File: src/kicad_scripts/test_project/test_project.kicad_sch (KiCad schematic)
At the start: 256 parts

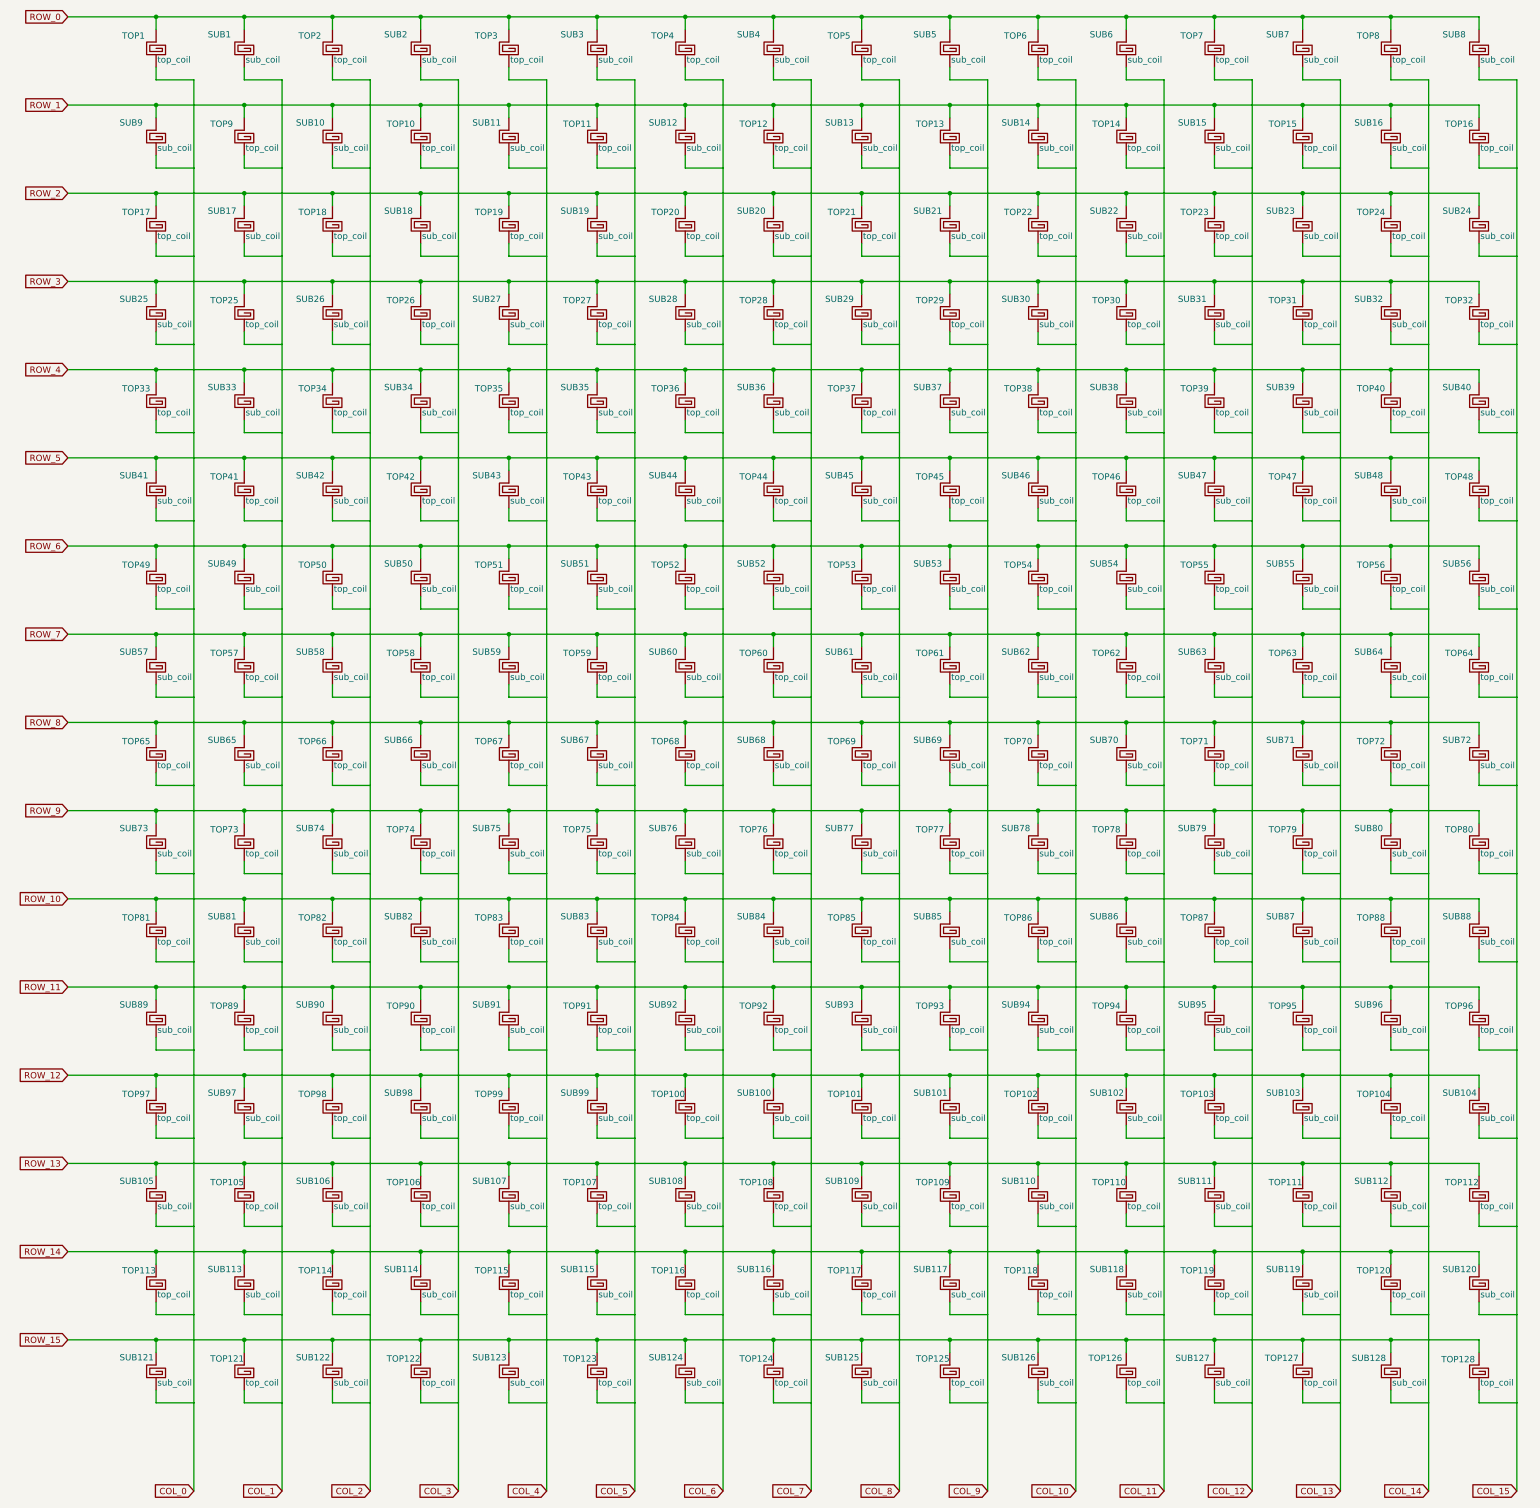
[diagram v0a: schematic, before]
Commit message: Added test project, lets go by hand for now
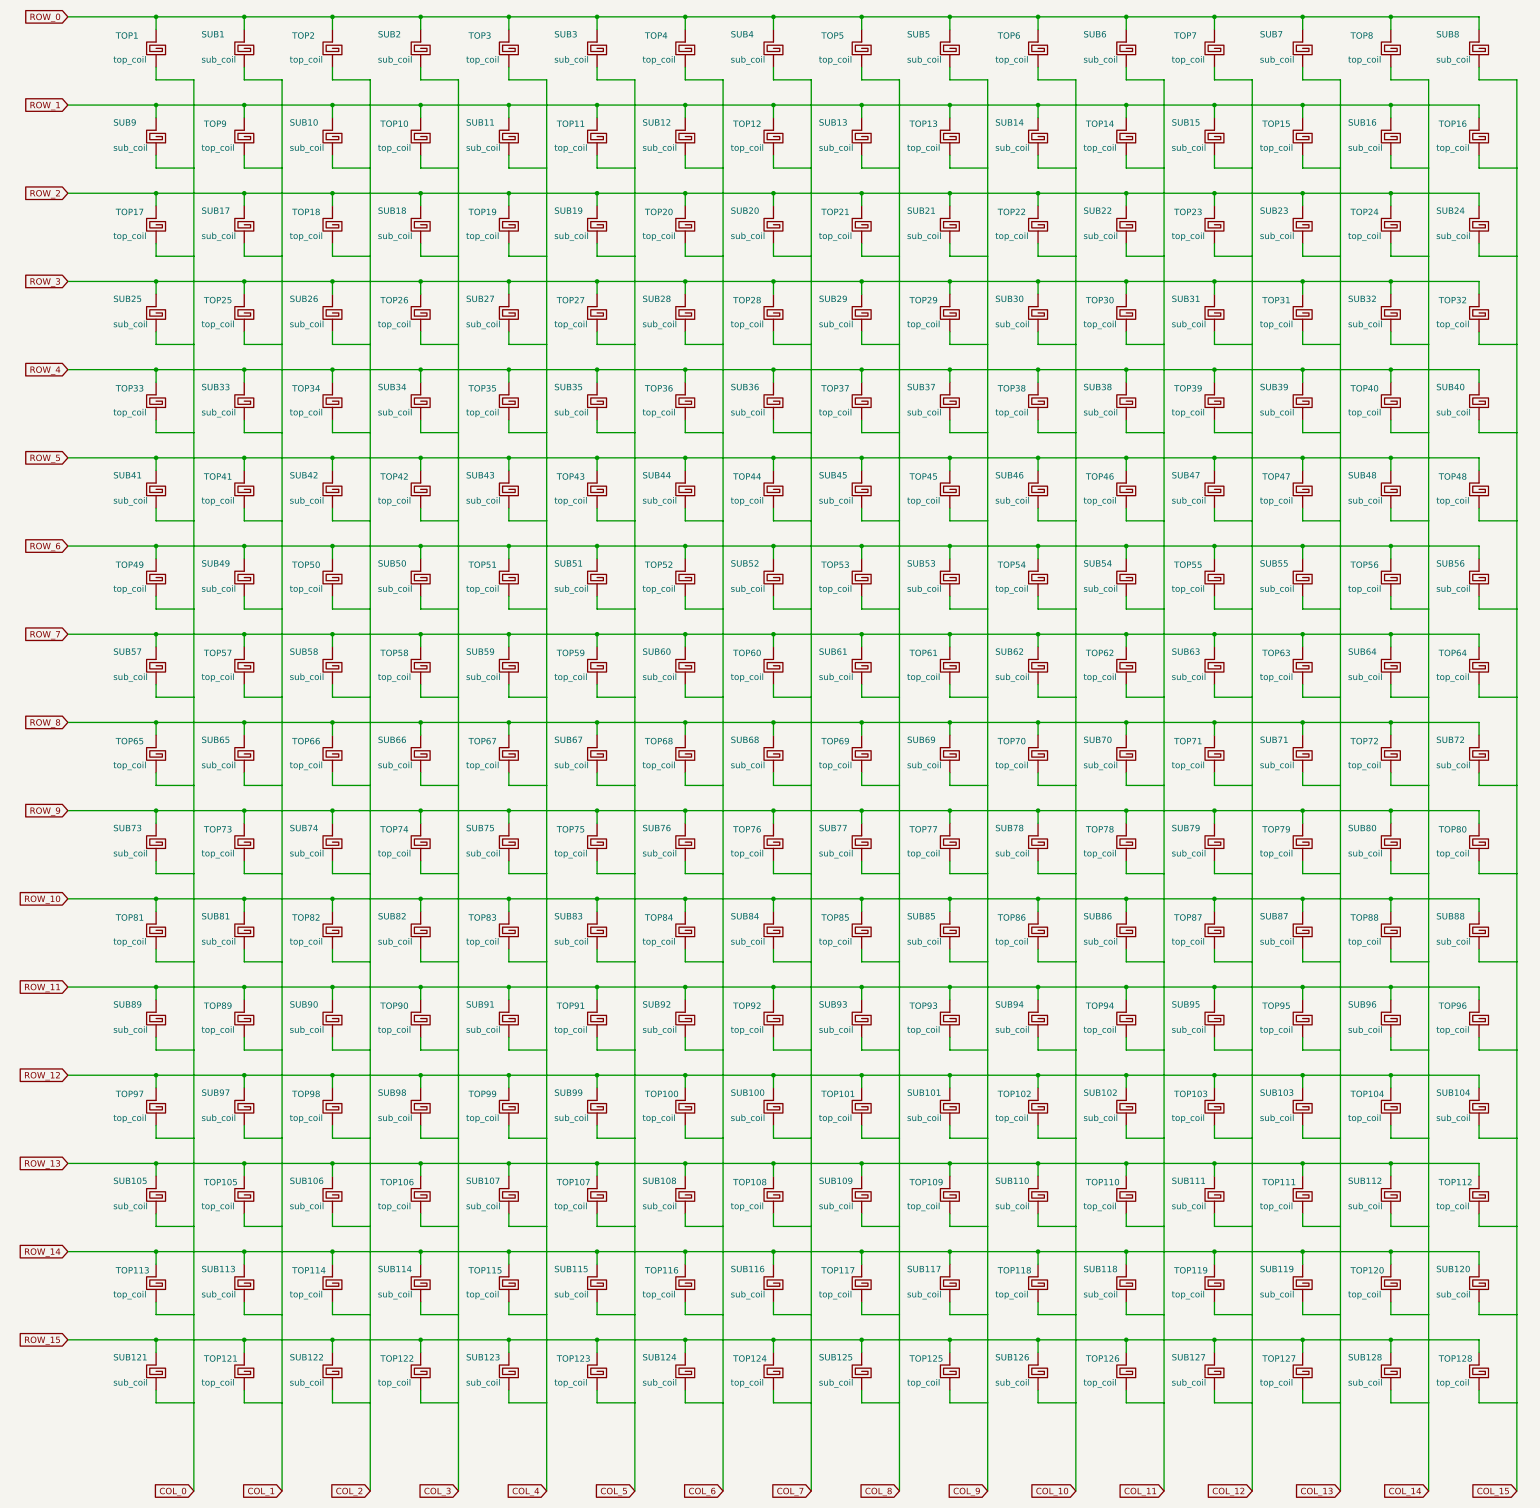
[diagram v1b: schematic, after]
